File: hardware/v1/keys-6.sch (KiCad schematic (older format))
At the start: 8 parts, among them P38 CONN_01X04, U10 MCP23017

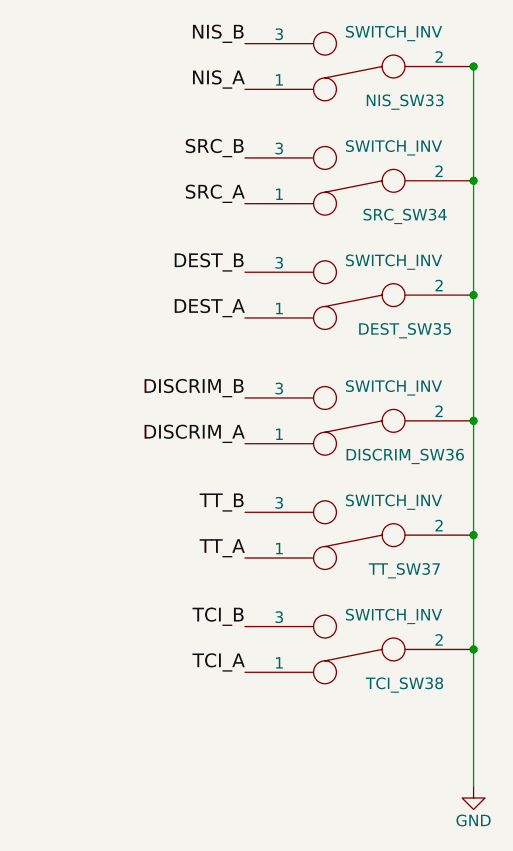
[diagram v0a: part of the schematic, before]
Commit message: Add pcbs and cutouts for magnetic drum store status lamps (not labelled).
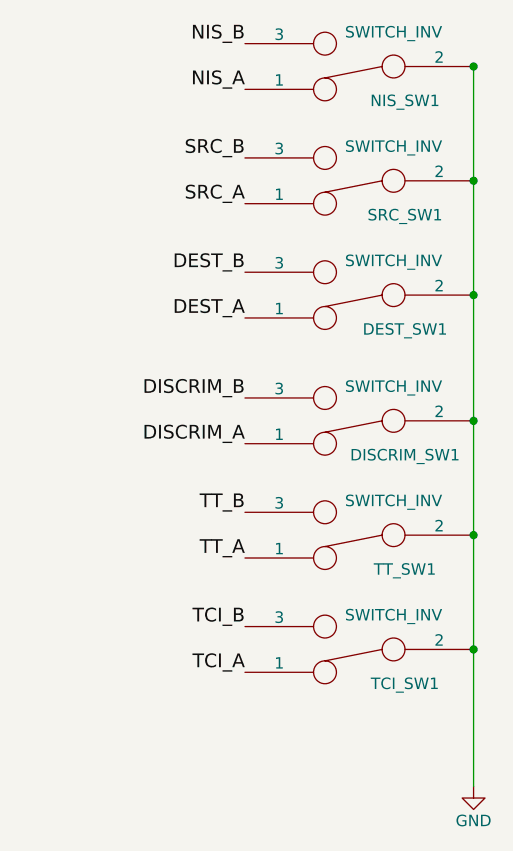
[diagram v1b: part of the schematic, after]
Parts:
- renumbered DEST_SW35 to DEST_SW1, DISCRIM_SW36 to DISCRIM_SW1, NIS_SW33 to NIS_SW1, SRC_SW34 to SRC_SW1, TCI_SW38 to TCI_SW1, TT_SW37 to TT_SW1
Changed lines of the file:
@@
 $Descr A4 11693 8268
 encoding utf-8
-Sheet 1 31
+Sheet 1 36
 Title ""
 Date ""
@@
 $EndDescr
 $Comp
-L SWITCH_INV DISCRIM_SW36
+L SWITCH_INV DISCRIM_SW1
 U 1 1 57AB8288
 P 9150 3500
-F 0 "DISCRIM_SW36" H 8950 3650 50  0000 C CNN
+F 0 "DISCRIM_SW1" H 8950 3650 50  0000 C CNN
 F 1 "SWITCH_INV" H 9000 3350 50  0000 C CNN
 F 2 "myparts:SW_SPDT-custom" H 9150 3500 50  0001 C CNN
@@
 $EndComp
 $Comp
-L SWITCH_INV TT_SW37
+L SWITCH_INV TT_SW1
 U 1 1 57AB828F
 P 9150 4000
-F 0 "TT_SW37" H 8950 4150 50  0000 C CNN
+F 0 "TT_SW1" H 8950 4150 50  0000 C CNN
 F 1 "SWITCH_INV" H 9000 3850 50  0000 C CNN
 F 2 "myparts:SW_SPDT-custom" H 9150 4000 50  0001 C CNN
@@
 $EndComp
 $Comp
-L SWITCH_INV TCI_SW38
+L SWITCH_INV TCI_SW1
 U 1 1 57AB8296
 P 9150 4500
-F 0 "TCI_SW38" H 8950 4650 50  0000 C CNN
+F 0 "TCI_SW1" H 8950 4650 50  0000 C CNN
 F 1 "SWITCH_INV" H 9000 4350 50  0000 C CNN
 F 2 "myparts:SW_SPDT-custom" H 9150 4500 50  0001 C CNN
@@
 Connection ~ 9650 4000
 $Comp
-L SWITCH_INV NIS_SW33
+L SWITCH_INV NIS_SW1
 U 1 1 57AB8A36
 P 9150 1950
-F 0 "NIS_SW33" H 8950 2100 50  0000 C CNN
+F 0 "NIS_SW1" H 8950 2100 50  0000 C CNN
 F 1 "SWITCH_INV" H 9000 1800 50  0000 C CNN
 F 2 "myparts:SW_SPDT-custom" H 9150 1950 50  0001 C CNN
@@
 $EndComp
 $Comp
-L SWITCH_INV SRC_SW34
+L SWITCH_INV SRC_SW1
 U 1 1 57AB8A3C
 P 9150 2450
-F 0 "SRC_SW34" H 8950 2600 50  0000 C CNN
+F 0 "SRC_SW1" H 8950 2600 50  0000 C CNN
 F 1 "SWITCH_INV" H 9000 2300 50  0000 C CNN
 F 2 "myparts:SW_SPDT-custom" H 9150 2450 50  0001 C CNN
@@
 $EndComp
 $Comp
-L SWITCH_INV DEST_SW35
+L SWITCH_INV DEST_SW1
 U 1 1 57AB8A42
 P 9150 2950
-F 0 "DEST_SW35" H 8950 3100 50  0000 C CNN
+F 0 "DEST_SW1" H 8950 3100 50  0000 C CNN
 F 1 "SWITCH_INV" H 9000 2800 50  0000 C CNN
 F 2 "myparts:SW_SPDT-custom" H 9150 2950 50  0001 C CNN
